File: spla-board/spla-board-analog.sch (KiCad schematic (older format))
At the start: 99 parts, among them J13 J_ANALOG, J14 J_AREF, J8 J_AREF_AMP, U51 ADC1173, U52 ADC1173, U53 ADC1173, U61 LMH6611, U62 LMH6611, U63 LMH6611, U74 LMH6611, U75 LMH6611, U76 TLV73333PDBV

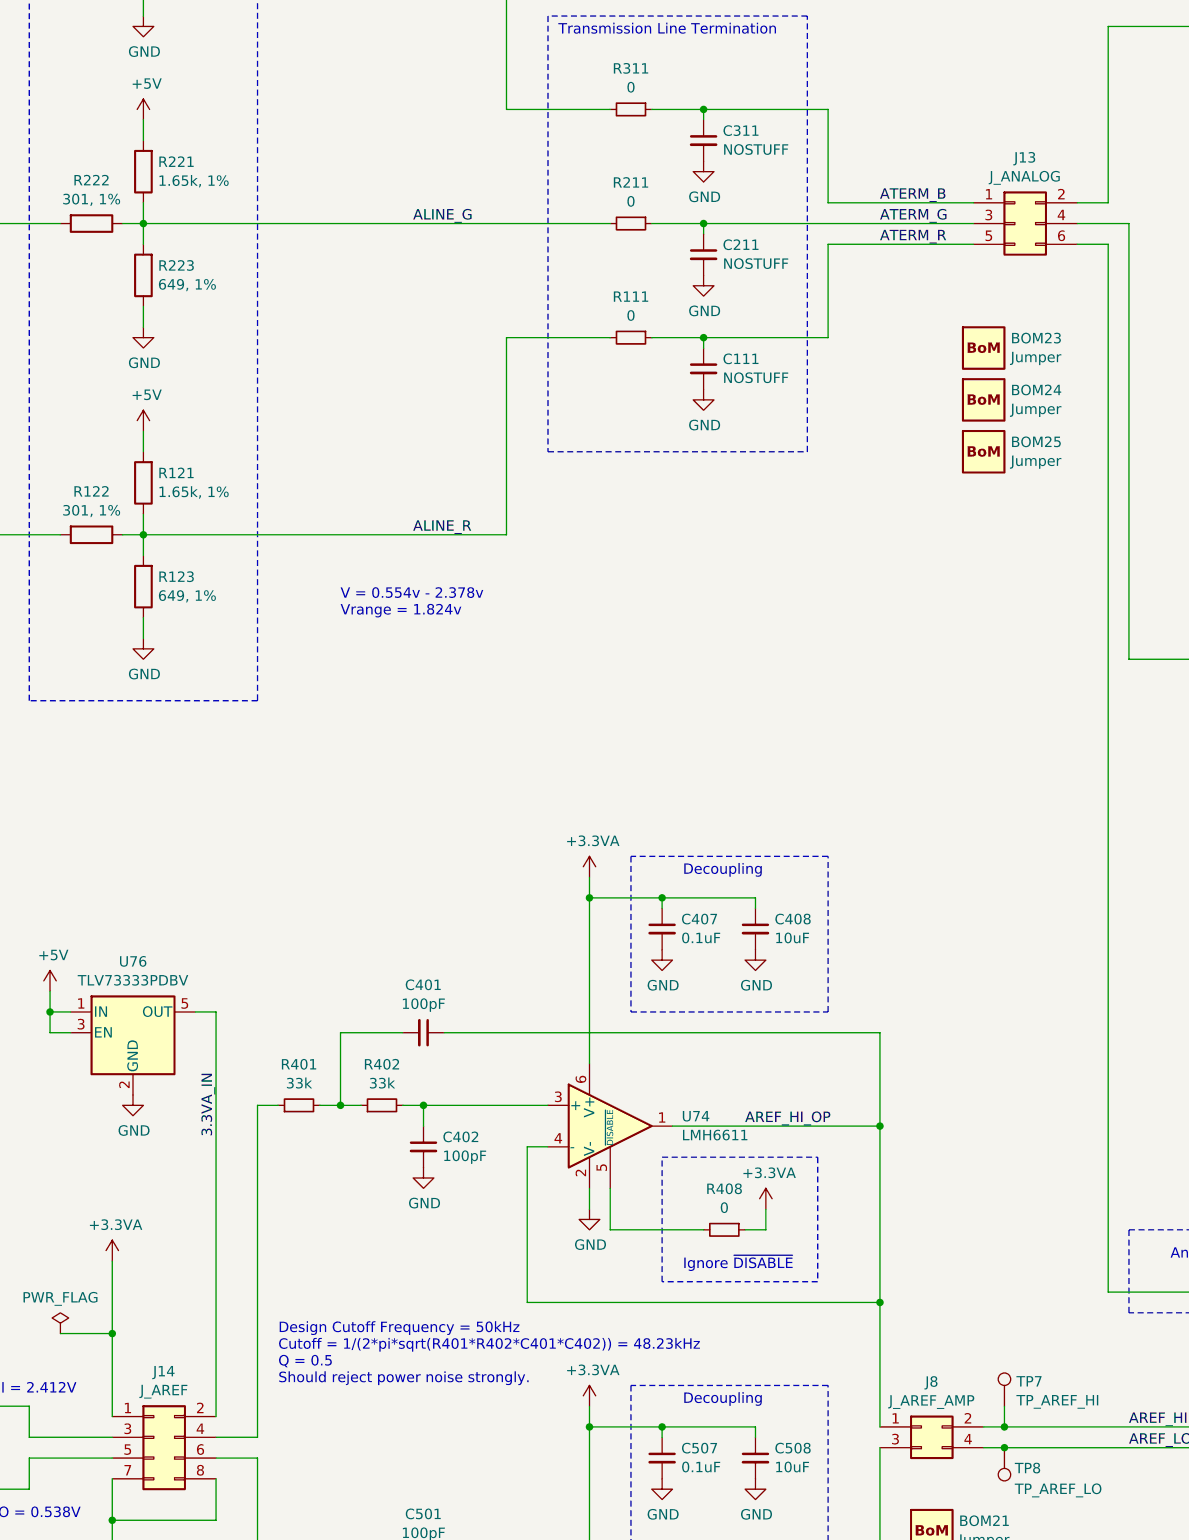
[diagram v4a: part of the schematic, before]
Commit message: schematic/pcb: Renumber connectors (J*).
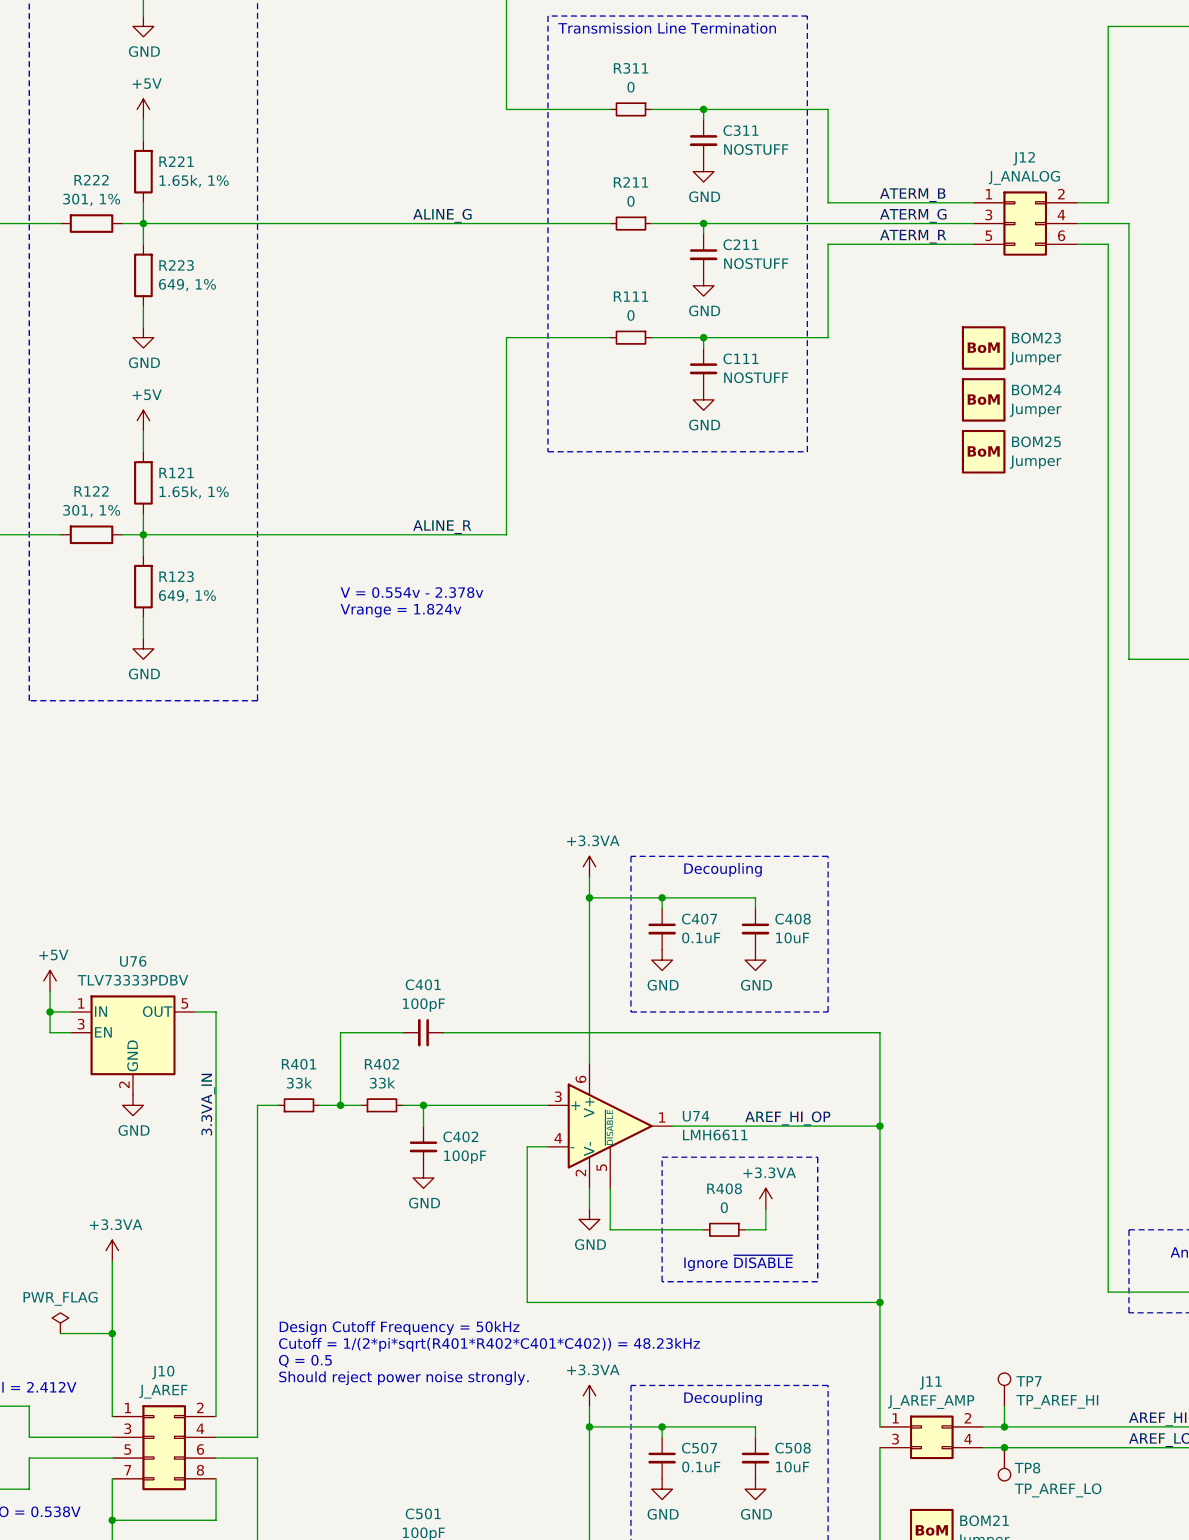
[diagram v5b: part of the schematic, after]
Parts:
- renumbered J14 to J10, J8 to J11, J13 to J12
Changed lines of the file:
@@
 	1900 8950 1500 8950
 $Comp
-L Connector_Generic:Conn_02x04_Odd_Even J14
+L Connector_Generic:Conn_02x04_Odd_Even J10
 U 1 1 5E5B71A2
 P 2100 8850
-F 0 "J14" H 2150 9167 50  0000 C CNN
+F 0 "J10" H 2150 9167 50  0000 C CNN
 F 1 "J_AREF" H 2150 9076 50  0000 C CNN
 F 2 "Connector_PinHeader_2.54mm:PinHeader_2x04_P2.54mm_Vertical" H 2100 8850 50  0001 C CNN
@@
 	1900 9250 1900 9350
 $Comp
-L Connector_Generic:Conn_02x03_Odd_Even J13
+L Connector_Generic:Conn_02x03_Odd_Even J12
 U 1 1 5E5CB713
 P 6250 3000
-F 0 "J13" H 6300 3317 50  0000 C CNN
+F 0 "J12" H 6300 3317 50  0000 C CNN
 F 1 "J_ANALOG" H 6300 3226 50  0000 C CNN
 F 2 "Connector_PinHeader_2.54mm:PinHeader_2x03_P2.54mm_Vertical" H 6250 3000 50  0001 C CNN
@@
 	6800 5100 7950 5100
 $Comp
-L Connector_Generic:Conn_02x02_Odd_Even J8
+L Connector_Generic:Conn_02x02_Odd_Even J11
 U 1 1 5EF0EE37
 P 5800 8800
-F 0 "J8" H 5850 9017 50  0000 C CNN
+F 0 "J11" H 5850 9017 50  0000 C CNN
 F 1 "J_AREF_AMP" H 5850 8926 50  0000 C CNN
 F 2 "Connector_PinHeader_2.54mm:PinHeader_2x02_P2.54mm_Vertical" H 5800 8800 50  0001 C CNN

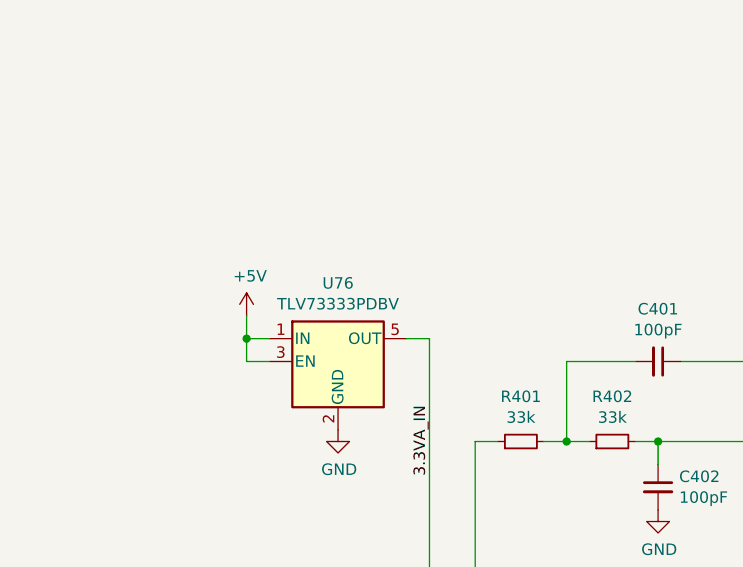
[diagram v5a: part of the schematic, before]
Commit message: schematic/pcb: Renumber level shifters.
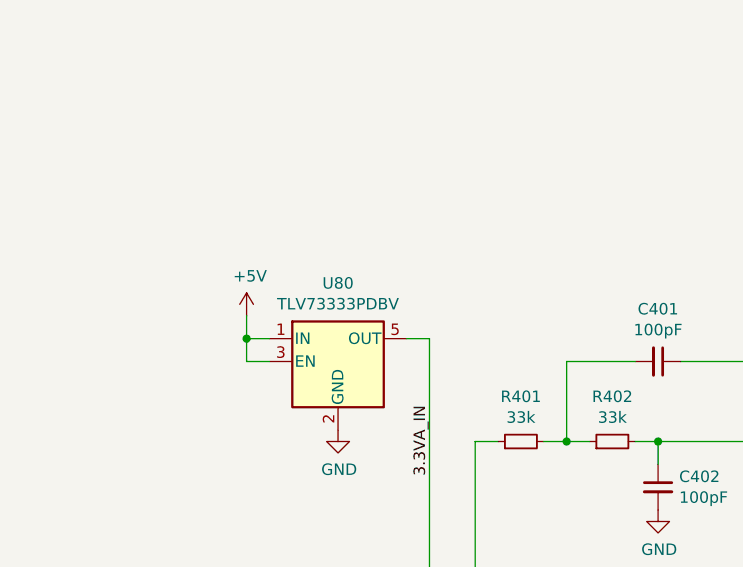
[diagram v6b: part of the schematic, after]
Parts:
- renumbered U76 to U80
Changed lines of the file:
@@
 	6200 8900 7250 8900
 $Comp
-L Regulator_Linear:TLV73333PDBV U76
+L Regulator_Linear:TLV73333PDBV U80
 U 1 1 5F3649E8
 P 2000 6900
-F 0 "U76" H 2000 7242 50  0000 C CNN
+F 0 "U80" H 2000 7242 50  0000 C CNN
 F 1 "TLV73333PDBV" H 2000 7151 50  0000 C CNN
 F 2 "Package_TO_SOT_SMD:SOT-23-5" H 2000 7100 50  0001 C CNN
